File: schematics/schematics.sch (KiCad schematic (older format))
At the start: 8 parts

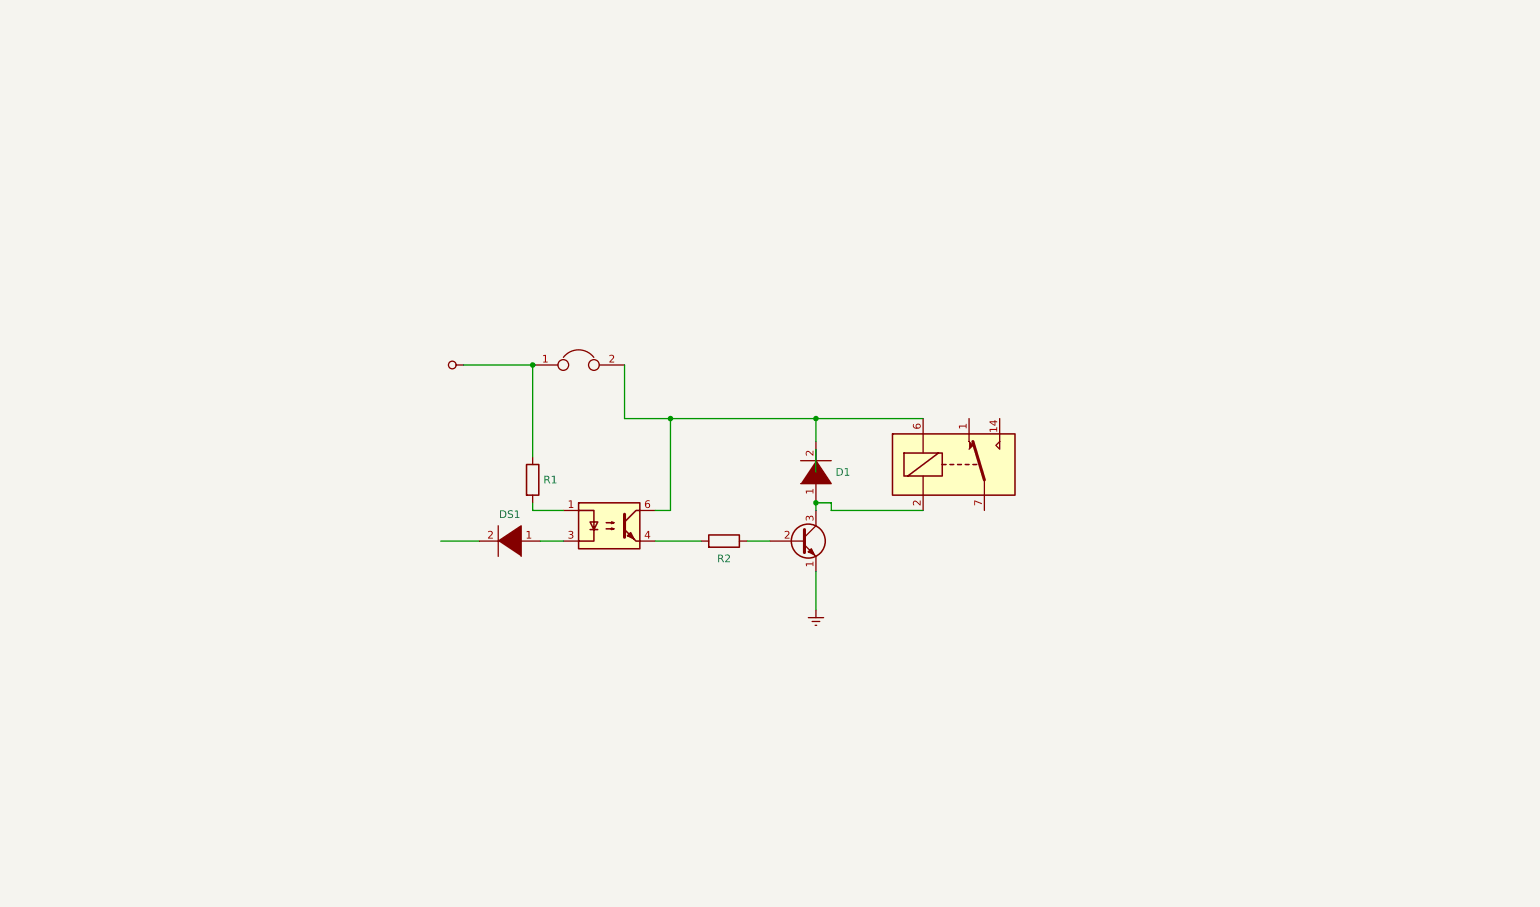
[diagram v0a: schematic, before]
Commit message: Add screw terminals
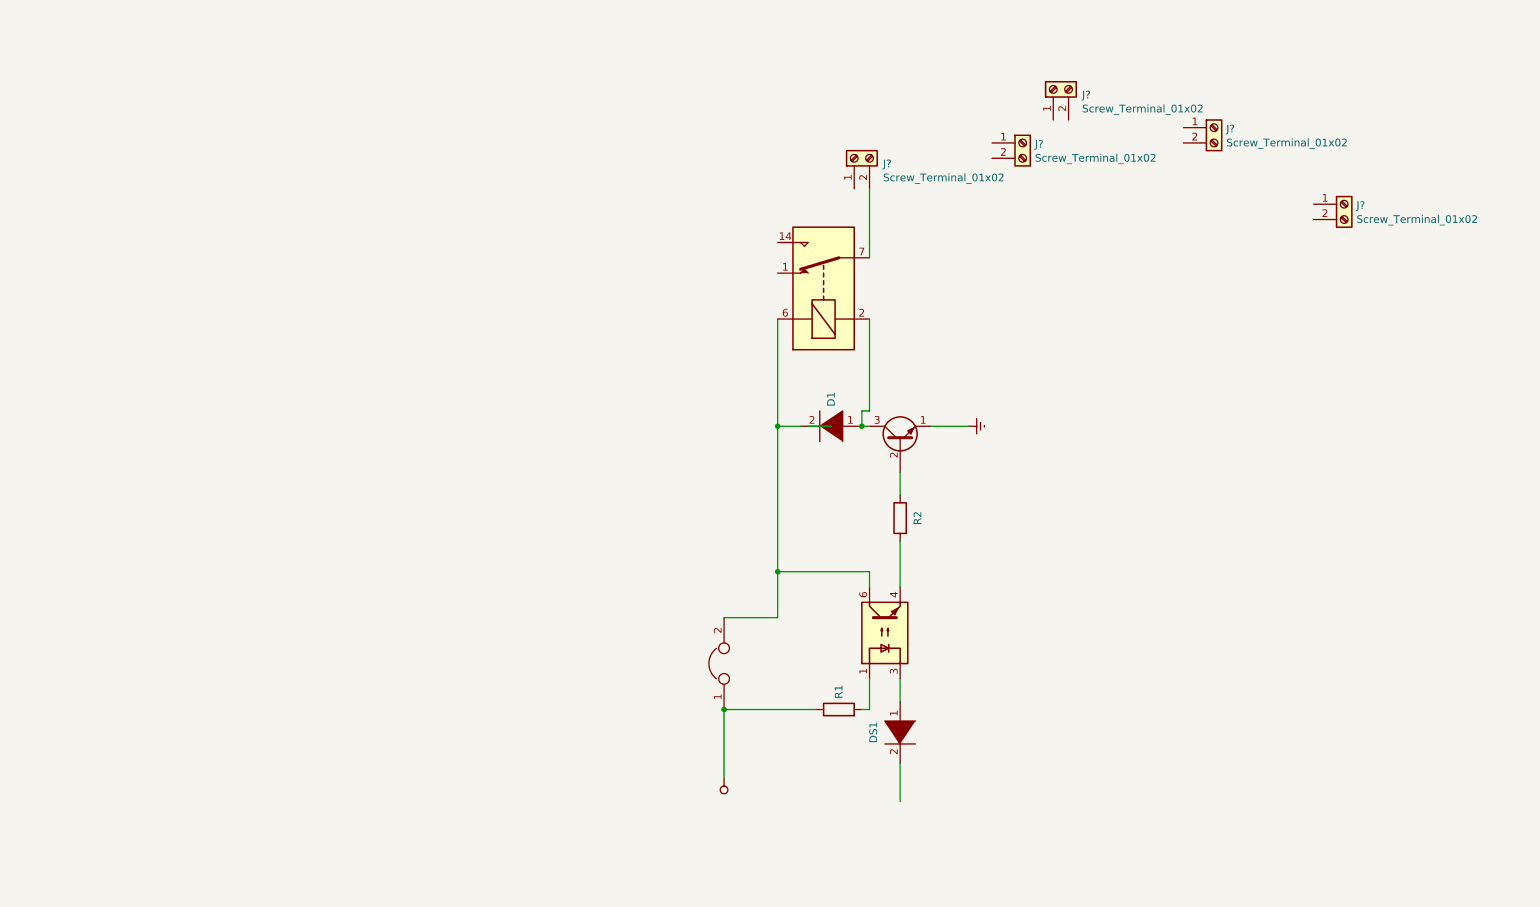
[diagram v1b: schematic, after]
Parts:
- added J? (x5): Screw_Terminal_01x02, symbol Connector:Screw_Terminal_01x02
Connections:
- wire segments 21 -> 22
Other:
- moved on the sheet: D1, R1, R2
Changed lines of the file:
@@
 $EndDescr
+$Comp
+L Connector:Screw_Terminal_01x02 J?
+U 1 1 5C8BD117
+P 8100 1750
+F 0 "J?" V 8064 1562 50  0000 R CNN
+F 1 "Screw_Terminal_01x02" V 7973 1562 50  0000 R CNN
+F 2 "" H 8100 1750 50  0001 C CNN
+F 3 "~" H 8100 1750 50  0001 C CNN
+	1    8100 1750
+	0    -1   -1   0
+$EndComp
+$Comp
+L Connector:Screw_Terminal_01x02 J?
+U 1 1 5C8BF337
+P 7900 2100
+F 0 "J?" H 7980 2092 50  0000 L CNN
+F 1 "Screw_Terminal_01x02" H 7980 2001 50  0000 L CNN
+F 2 "" H 7900 2100 50  0001 C CNN
+F 3 "~" H 7900 2100 50  0001 C CNN
+	1    7900 2100
+	1    0    0    -1
+$EndComp
+$Comp
+L Connector:Screw_Terminal_01x02 J?
+U 1 1 5C8BF7F8
+P 9150 2000
+F 0 "J?" H 9230 1992 50  0000 L CNN
+F 1 "Screw_Terminal_01x02" H 9230 1901 50  0000 L CNN
+F 2 "" H 9150 2000 50  0001 C CNN
+F 3 "~" H 9150 2000 50  0001 C CNN
+	1    9150 2000
+	1    0    0    -1
+$EndComp
+$Comp
+L Connector:Screw_Terminal_01x02 J?
+U 1 1 5C8BFD9E
+P 10000 2500
+F 0 "J?" H 10080 2492 50  0000 L CNN
+F 1 "Screw_Terminal_01x02" H 10080 2401 50  0000 L CNN
+F 2 "" H 10000 2500 50  0001 C CNN
+F 3 "~" H 10000 2500 50  0001 C CNN
+	1    10000 2500
+	1    0    0    -1
+$EndComp
 $Comp
 L Device:R R1
 U 1 1 5C8BA970
-P 4700 4300
-F 0 "R1" H 4770 4300 50  0000 L CNN
-F 1 "R" H 4770 4255 50  0001 L CNN
-F 2 "" V 4630 4300 50  0001 C CNN
-F 3 "~" H 4700 4300 50  0001 C CNN
-	1    4700 4300
-	1    0    0    -1
-$EndComp
-Wire Wire Line
-	4700 4450 4700 4500
-Wire Wire Line
-	4700 4500 4900 4500
+P 6700 5800
+F 0 "R1" H 6770 5800 50  0000 L CNN
+F 1 "R" H 6770 5755 50  0001 L CNN
+F 2 "" V 6630 5800 50  0001 C CNN
+F 3 "~" H 6700 5800 50  0001 C CNN
+	1    6700 5800
+	0    -1   -1   0
+$EndComp
+Wire Wire Line
+	6850 5800 6900 5800
+Wire Wire Line
+	6900 5800 6900 5600
 $Comp
 L Isolator:TLP185 U?
 U 1 1 5C8BCBB8
-P 5200 4600
-F 0 "U?" H 5200 4925 50  0001 C CNN
-F 1 "TLP185" H 5200 4833 50  0001 C CNN
-F 2 "Package_SO:SOIC-4_4.55x3.7mm_P2.54mm" H 5200 4300 50  0001 C CIN
-F 3 "https://toshiba.semicon-storage.com/info/docget.jsp?did=11791&prodName=TLP185" H 5200 4600 50  0001 L CNN
-	1    5200 4600
-	1    0    0    -1
-$EndComp
-Wire Wire Line
-	4900 4700 4750 4700
+P 7000 5300
+F 0 "U?" H 7000 5625 50  0001 C CNN
+F 1 "TLP185" H 7000 5533 50  0001 C CNN
+F 2 "Package_SO:SOIC-4_4.55x3.7mm_P2.54mm" H 7000 5000 50  0001 C CIN
+F 3 "https://toshiba.semicon-storage.com/info/docget.jsp?did=11791&prodName=TLP185" H 7000 5300 50  0001 L CNN
+	1    7000 5300
+	0    -1   -1   0
+$EndComp
+Wire Wire Line
+	7100 5600 7100 5750
 $Comp
 L pspice:DIODE D?
 U 1 1 5C8C1EFD
-P 4550 4700
-F 0 "D?" H 4550 4435 50  0001 C CNN
-F 1 "DS1" H 4550 4526 50  0000 C CNN
-F 2 "" H 4550 4700 50  0001 C CNN
-F 3 "~" H 4550 4700 50  0001 C CNN
-	1    4550 4700
-	-1   0    0    1
-$EndComp
-Wire Wire Line
-	4350 4700 4100 4700
-Wire Wire Line
-	5500 4700 5800 4700
+P 7100 5950
+F 0 "D?" H 7100 5685 50  0001 C CNN
+F 1 "DS1" H 7100 5776 50  0000 C CNN
+F 2 "" H 7100 5950 50  0001 C CNN
+F 3 "~" H 7100 5950 50  0001 C CNN
+	1    7100 5950
+	0    1    1    0
+$EndComp
+Wire Wire Line
+	7100 6150 7100 6400
+Wire Wire Line
+	7100 5000 7100 4700
 $Comp
 L Device:R R2
 U 1 1 5C8C515D
-P 5950 4700
-F 0 "R2" V 5835 4700 50  0000 C CNN
-F 1 "R" V 5834 4700 50  0001 C CNN
-F 2 "" V 5880 4700 50  0001 C CNN
-F 3 "~" H 5950 4700 50  0001 C CNN
-	1    5950 4700
-	0    1    -1   0
-$EndComp
-Wire Wire Line
-	6100 4700 6250 4700
+P 7100 4550
+F 0 "R2" V 6985 4550 50  0000 C CNN
+F 1 "R" V 6984 4550 50  0001 C CNN
+F 2 "" V 7030 4550 50  0001 C CNN
+F 3 "~" H 7100 4550 50  0001 C CNN
+	1    7100 4550
+	-1   0    0    -1
+$EndComp
+Wire Wire Line
+	7100 4400 7100 4250
 $Comp
 L Transistor_BJT:2N2219 Q?
 U 1 1 5C8C7983
-P 6450 4700
-F 0 "Q?" H 6640 4746 50  0001 L CNN
-F 1 "2N2219" H 6640 4700 50  0001 L CNN
-F 2 "Package_TO_SOT_THT:TO-39-3" H 6650 4625 50  0001 L CIN
-F 3 "http://www.onsemi.com/pub_link/Collateral/2N2219-D.PDF" H 6450 4700 50  0001 L CNN
-	1    6450 4700
-	1    0    0    -1
-$EndComp
-Wire Wire Line
-	6550 4900 6550 5150
+P 7100 4050
+F 0 "Q?" H 7290 4096 50  0001 L CNN
+F 1 "2N2219" H 7290 4050 50  0001 L CNN
+F 2 "Package_TO_SOT_THT:TO-39-3" H 7300 3975 50  0001 L CIN
+F 3 "http://www.onsemi.com/pub_link/Collateral/2N2219-D.PDF" H 7100 4050 50  0001 L CNN
+	1    7100 4050
+	0    -1   -1   0
+$EndComp
+Wire Wire Line
+	7300 3950 7550 3950
 $Comp
 L power:GNDREF #PWR?
 U 1 1 5C8C8969
-P 6550 5150
-F 0 "#PWR?" H 6550 4900 50  0001 C CNN
-F 1 "GNDREF" H 6555 4977 50  0001 C CNN
-F 2 "" H 6550 5150 50  0001 C CNN
-F 3 "" H 6550 5150 50  0001 C CNN
-	1    6550 5150
-	1    0    0    -1
-$EndComp
-Wire Wire Line
-	4700 3550 4250 3550
+P 7550 3950
+F 0 "#PWR?" H 7550 3700 50  0001 C CNN
+F 1 "GNDREF" H 7555 3777 50  0001 C CNN
+F 2 "" H 7550 3950 50  0001 C CNN
+F 3 "" H 7550 3950 50  0001 C CNN
+	1    7550 3950
+	0    -1   -1   0
+$EndComp
+Wire Wire Line
+	5950 5800 5950 6250
 $Comp
 L power:VCC #PWR?
 U 1 1 5C8BE04C
-P 4250 3550
-F 0 "#PWR?" H 4250 3400 50  0001 C CNN
-F 1 "VCC" V 4268 3677 50  0001 L CNN
-F 2 "" H 4250 3550 50  0001 C CNN
-F 3 "" H 4250 3550 50  0001 C CNN
-	1    4250 3550
-	0    -1   -1   0
-$EndComp
-Wire Wire Line
-	5500 4500 5600 4500
-Wire Wire Line
-	6550 4500 6550 4450
+P 5950 6250
+F 0 "#PWR?" H 5950 6100 50  0001 C CNN
+F 1 "VCC" V 5968 6377 50  0001 L CNN
+F 2 "" H 5950 6250 50  0001 C CNN
+F 3 "" H 5950 6250 50  0001 C CNN
+	1    5950 6250
+	-1   0    0    1
+$EndComp
+Wire Wire Line
+	6900 5000 6900 4900
+Wire Wire Line
+	6900 3950 6850 3950
 $Comp
 L pspice:DIODE D1
 U 1 1 5C8C3A6E
-P 6550 4250
-F 0 "D1" V 6550 4122 50  0000 R CNN
-F 1 "DIODE" V 6505 4122 50  0001 R CNN
-F 2 "" H 6550 4250 50  0001 C CNN
-F 3 "~" H 6550 4250 50  0001 C CNN
-	1    6550 4250
-	0    -1   -1   0
-$EndComp
-Wire Wire Line
-	6550 4100 6550 4250
+P 6650 3950
+F 0 "D1" V 6650 3822 50  0000 R CNN
+F 1 "DIODE" V 6605 3822 50  0001 R CNN
+F 2 "" H 6650 3950 50  0001 C CNN
+F 3 "~" H 6650 3950 50  0001 C CNN
+	1    6650 3950
+	-1   0    0    1
+$EndComp
+Wire Wire Line
+	6500 3950 6650 3950
 $Comp
 L Device:Jumper JP?
 U 1 1 5C8CFC95
-P 5000 3550
-F 0 "JP?" H 5000 3814 50  0001 C CNN
-F 1 "Jumper" H 5000 3723 50  0001 C CNN
-F 2 "" H 5000 3550 50  0001 C CNN
-F 3 "~" H 5000 3550 50  0001 C CNN
-	1    5000 3550
-	1    0    0    -1
+P 5950 5500
+F 0 "JP?" H 5950 5764 50  0001 C CNN
+F 1 "Jumper" H 5950 5673 50  0001 C CNN
+F 2 "" H 5950 5500 50  0001 C CNN
+F 3 "~" H 5950 5500 50  0001 C CNN
+	1    5950 5500
+	0    -1   -1   0
 $EndComp
 $Comp
 L Relay:DIPxx-1Cxx-51x K?
 U 1 1 5C8D3DB8
-P 7450 4200
-F 0 "K?" H 7880 4246 50  0001 L CNN
-F 1 "DIPxx-1Cxx-51x" H 7880 4200 50  0001 L CNN
-F 2 "Relay_THT:Relay_StandexMeder_DIP_LowProfile" H 7900 4150 50  0001 L CNN
-F 3 "https://standexelectronics.com/wp-content/uploads/datasheet_reed_relay_DIP.pdf" H 7450 4200 50  0001 C CNN
-	1    7450 4200
-	1    0    0    -1
-$EndComp
-Wire Wire Line
-	5300 3900 5600 3900
-Wire Wire Line
-	5300 3550 5300 3900
-Wire Wire Line
-	6550 4050 6550 3900
-Wire Wire Line
-	4700 3550 4700 4150
-Connection ~ 4700 3550
-Wire Wire Line
-	5600 3900 5600 4500
-Connection ~ 5600 3900
-Wire Wire Line
-	5600 3900 6550 3900
-Wire Wire Line
-	7250 3900 6550 3900
-Connection ~ 6550 3900
-Wire Wire Line
-	7250 4500 6650 4500
-Wire Wire Line
-	6650 4500 6650 4450
-Wire Wire Line
-	6650 4450 6550 4450
-Connection ~ 6550 4450
+P 6600 3050
+F 0 "K?" H 7030 3096 50  0001 L CNN
+F 1 "DIPxx-1Cxx-51x" H 7030 3050 50  0001 L CNN
+F 2 "Relay_THT:Relay_StandexMeder_DIP_LowProfile" H 7050 3000 50  0001 L CNN
+F 3 "https://standexelectronics.com/wp-content/uploads/datasheet_reed_relay_DIP.pdf" H 6600 3050 50  0001 C CNN
+	1    6600 3050
+	0    -1   -1   0
+$EndComp
+Wire Wire Line
+	6300 5200 6300 4900
+Wire Wire Line
+	5950 5200 6300 5200
+Wire Wire Line
+	6450 3950 6300 3950
+Wire Wire Line
+	5950 5800 6550 5800
+Connection ~ 5950 5800
+Wire Wire Line
+	6300 4900 6900 4900
+Connection ~ 6300 4900
+Wire Wire Line
+	6300 4900 6300 3950
+Wire Wire Line
+	6300 3250 6300 3950
+Connection ~ 6300 3950
+Wire Wire Line
+	6900 3250 6900 3850
+Wire Wire Line
+	6900 3850 6850 3850
+Wire Wire Line
+	6850 3850 6850 3950
+Connection ~ 6850 3950
+$Comp
+L Connector:Screw_Terminal_01x02 J?
+U 1 1 5C8BEC1E
+P 6800 2200
+F 0 "J?" V 6764 2012 50  0000 R CNN
+F 1 "Screw_Terminal_01x02" V 6673 2012 50  0000 R CNN
+F 2 "" H 6800 2200 50  0001 C CNN
+F 3 "~" H 6800 2200 50  0001 C CNN
+	1    6800 2200
+	0    -1   -1   0
+$EndComp
+Wire Wire Line
+	6900 2400 6900 2850
 $EndSCHEMATC

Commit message: Add the base for all pumps with screw terminals
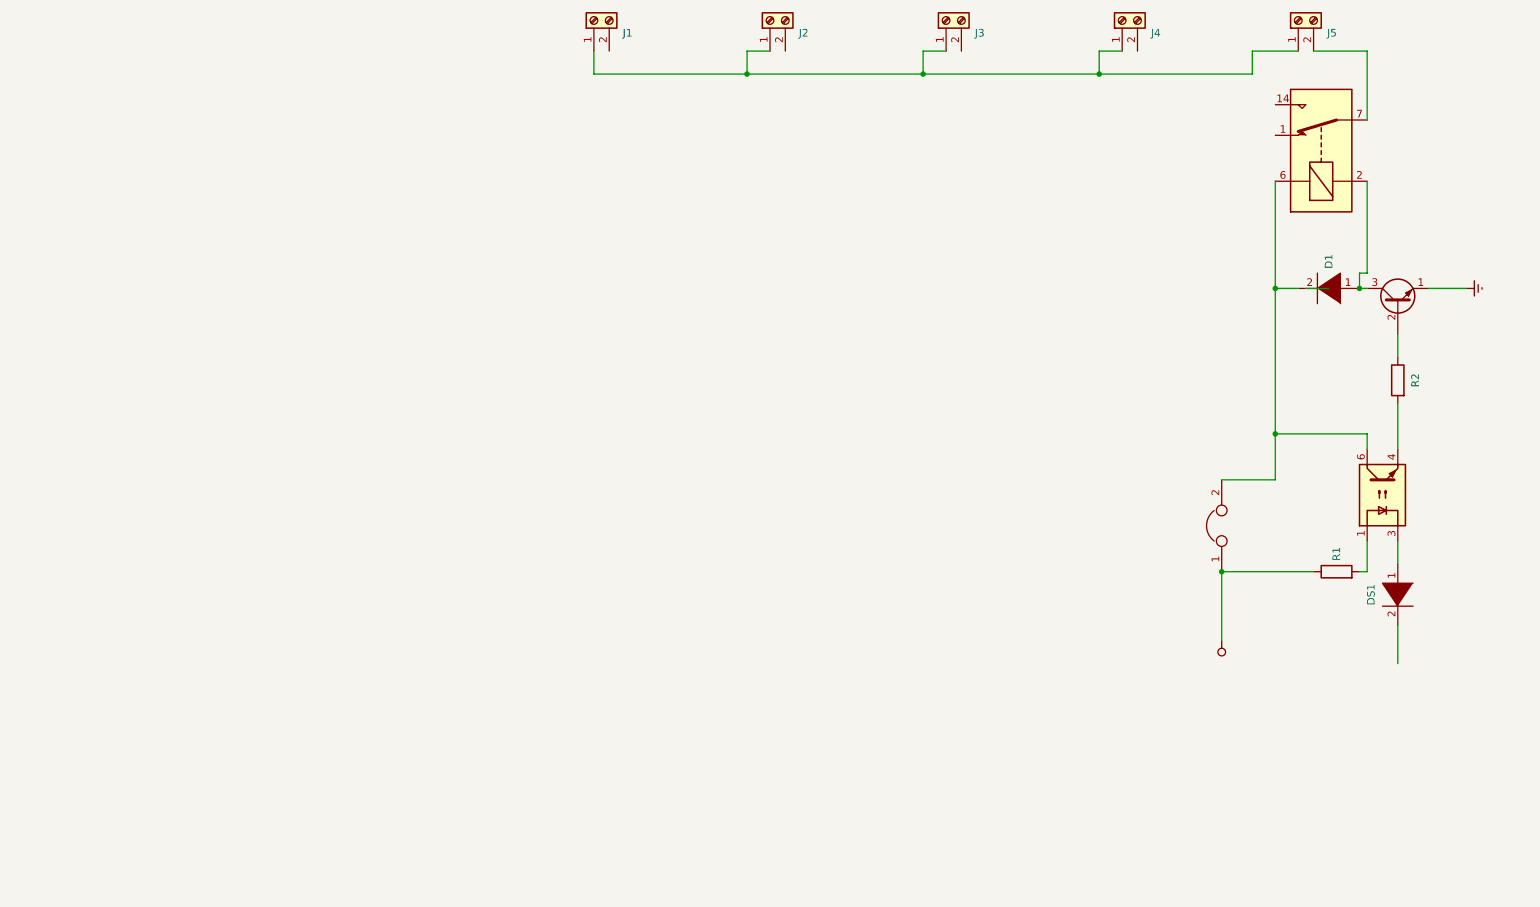
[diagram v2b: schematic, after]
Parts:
- gave numbers to parts that had none: 5
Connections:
- wire segments 22 -> 36
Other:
- moved on the sheet: D1, J1, J2, J3, J4, J5, R1, R2
